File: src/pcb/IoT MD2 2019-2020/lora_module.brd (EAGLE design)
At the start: 25.4 x 31.4 mm, 7 parts, among them J1 U.FL-R-SMT-1(10)

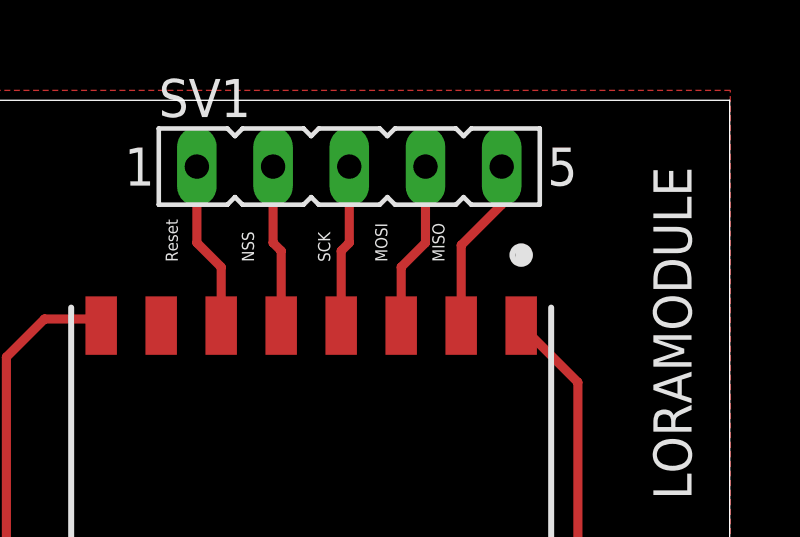
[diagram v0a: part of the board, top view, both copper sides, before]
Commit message: Updated lora scheme
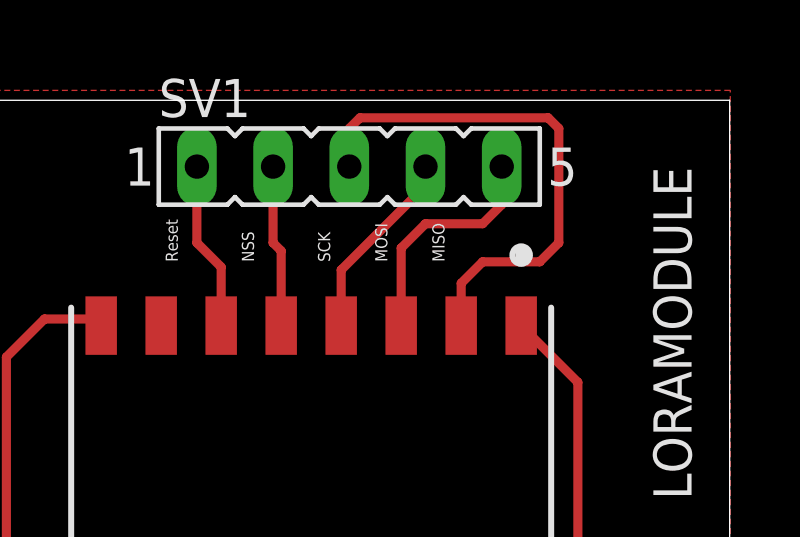
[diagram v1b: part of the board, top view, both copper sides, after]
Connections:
- net MISO: now also SV1.3; no longer SV1.5
- net MOSI: now also SV1.5; no longer SV1.4
- net SCK: now also SV1.4; no longer SV1.3
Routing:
- net MISO: track 5.86 -> 17.6 mm
- net MOSI: track 5.64 -> 7.80 mm
- net SCK: track 5.41 -> 6.46 mm
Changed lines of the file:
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@@
 <?xml version="1.0" encoding="utf-8"?>
 <!DOCTYPE eagle SYSTEM "eagle.dtd">
-<eagle version="9.5.0">
+<eagle version="9.5.1">
 <drawing>
 <settings>
@@
 <signal name="MOSI">
 <contactref element="LORAMODULE" pad="3"/>
-<contactref element="SV1" pad="4"/>
-<wire x1="15.7" y1="62.01" x2="15.7" y2="63.96" width="0.3048" layer="1"/>
-<wire x1="15.7" y1="63.96" x2="16.51" y2="64.77" width="0.3048" layer="1"/>
-<wire x1="16.51" y1="64.77" x2="16.51" y2="67.31" width="0.3048" layer="1"/>
+<contactref element="SV1" pad="5"/>
+<wire x1="19.05" y1="67.31" x2="19.05" y2="66.04" width="0.3048" layer="1"/>
+<wire x1="19.05" y1="66.04" x2="18.415" y2="65.405" width="0.3048" layer="1"/>
+<wire x1="18.415" y1="65.405" x2="16.51" y2="65.405" width="0.3048" layer="1"/>
+<wire x1="15.7" y1="64.595" x2="15.7" y2="62.01" width="0.3048" layer="1"/>
+<wire x1="16.51" y1="65.405" x2="15.7" y2="64.595" width="0.3048" layer="1"/>
 </signal>
 <signal name="RESET_LORA">
@@
 <signal name="SCK">
 <contactref element="LORAMODULE" pad="4"/>
-<contactref element="SV1" pad="3"/>
-<wire x1="13.7" y1="62.01" x2="13.7" y2="64.5" width="0.3048" layer="1"/>
-<wire x1="13.7" y1="64.5" x2="13.97" y2="64.77" width="0.3048" layer="1"/>
-<wire x1="13.97" y1="64.77" x2="13.97" y2="67.31" width="0.3048" layer="1"/>
+<contactref element="SV1" pad="4"/>
+<wire x1="16.51" y1="67.31" x2="16.51" y2="66.675" width="0.3048" layer="1"/>
+<wire x1="16.51" y1="66.675" x2="13.7" y2="63.865" width="0.3048" layer="1"/>
+<wire x1="13.7" y1="63.865" x2="13.7" y2="62.01" width="0.3048" layer="1"/>
 </signal>
 <signal name="NSS">
@@
 <signal name="MISO">
 <contactref element="LORAMODULE" pad="2"/>
-<contactref element="SV1" pad="5"/>
-<wire x1="17.7" y1="62.01" x2="17.7" y2="64.69" width="0.3048" layer="1"/>
-<wire x1="17.7" y1="64.69" x2="19.05" y2="66.04" width="0.3048" layer="1"/>
-<wire x1="19.05" y1="66.04" x2="19.05" y2="67.31" width="0.3048" layer="1"/>
+<contactref element="SV1" pad="3"/>
+<wire x1="13.97" y1="67.31" x2="13.97" y2="68.58" width="0.3048" layer="1"/>
+<wire x1="14.3256" y1="68.9356" x2="20.5994" y2="68.9356" width="0.3048" layer="1"/>
+<wire x1="20.5994" y1="68.9356" x2="20.955" y2="68.58" width="0.3048" layer="1"/>
+<wire x1="20.955" y1="64.77" x2="20.32" y2="64.135" width="0.3048" layer="1"/>
+<wire x1="20.32" y1="64.135" x2="18.415" y2="64.135" width="0.3048" layer="1"/>
+<wire x1="17.7" y1="63.42" x2="17.7" y2="62.01" width="0.3048" layer="1"/>
+<wire x1="13.97" y1="68.58" x2="14.3256" y2="68.9356" width="0.3048" layer="1"/>
+<wire x1="20.955" y1="68.58" x2="20.955" y2="64.77" width="0.3048" layer="1"/>
+<wire x1="18.415" y1="64.135" x2="17.7" y2="63.42" width="0.3048" layer="1"/>
 </signal>
 <signal name="VDD">
